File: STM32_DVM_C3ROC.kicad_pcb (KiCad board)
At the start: 4 copper layers, 110 x 56 mm, 174 parts, among them IC2 MCP6002, IC3 MCP6002, IC4 MCP6002, J1 40HAT, J2 USB_B_Micro, Q1 Crystal_GND24, SW1 SW_Push, T1 MMUN2214, T2 MMUN2214, T3 MMUN2214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

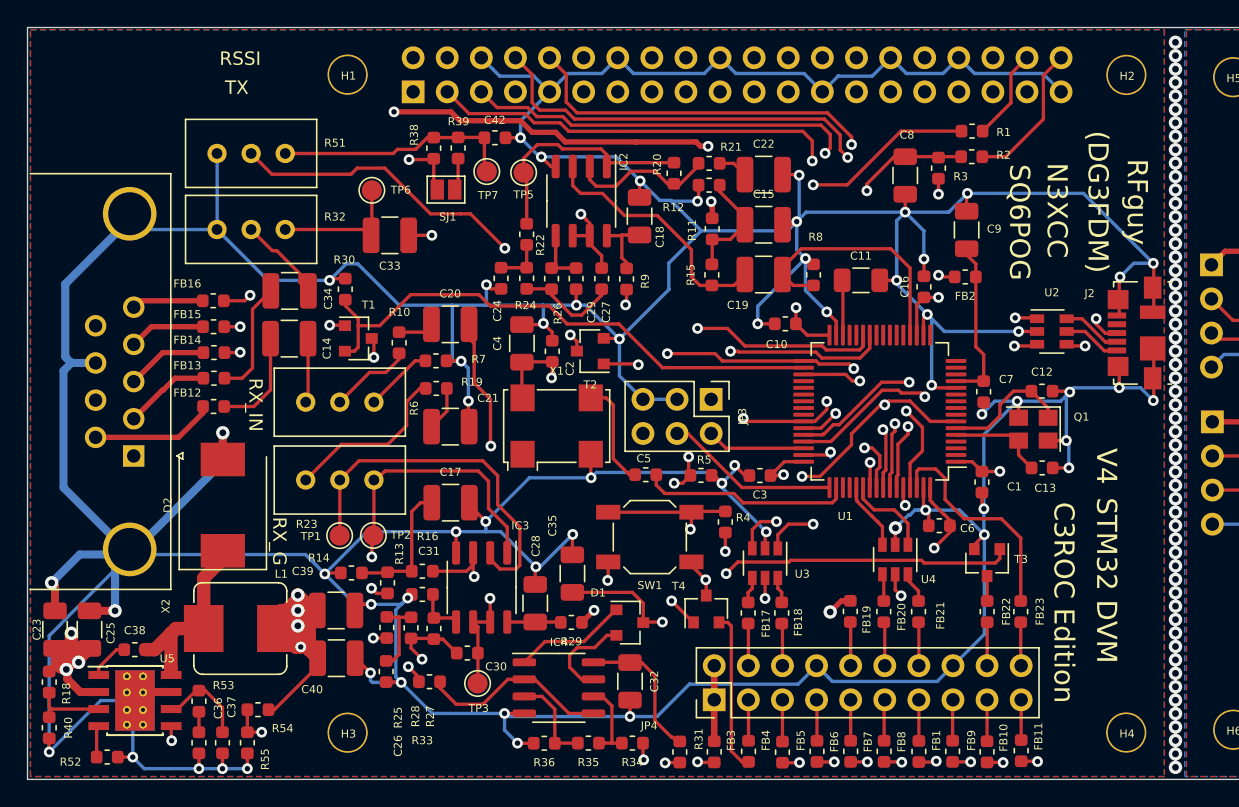
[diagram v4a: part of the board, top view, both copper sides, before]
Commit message: Layout fertig, Produktionsdaten für JCLPCB erzeugt
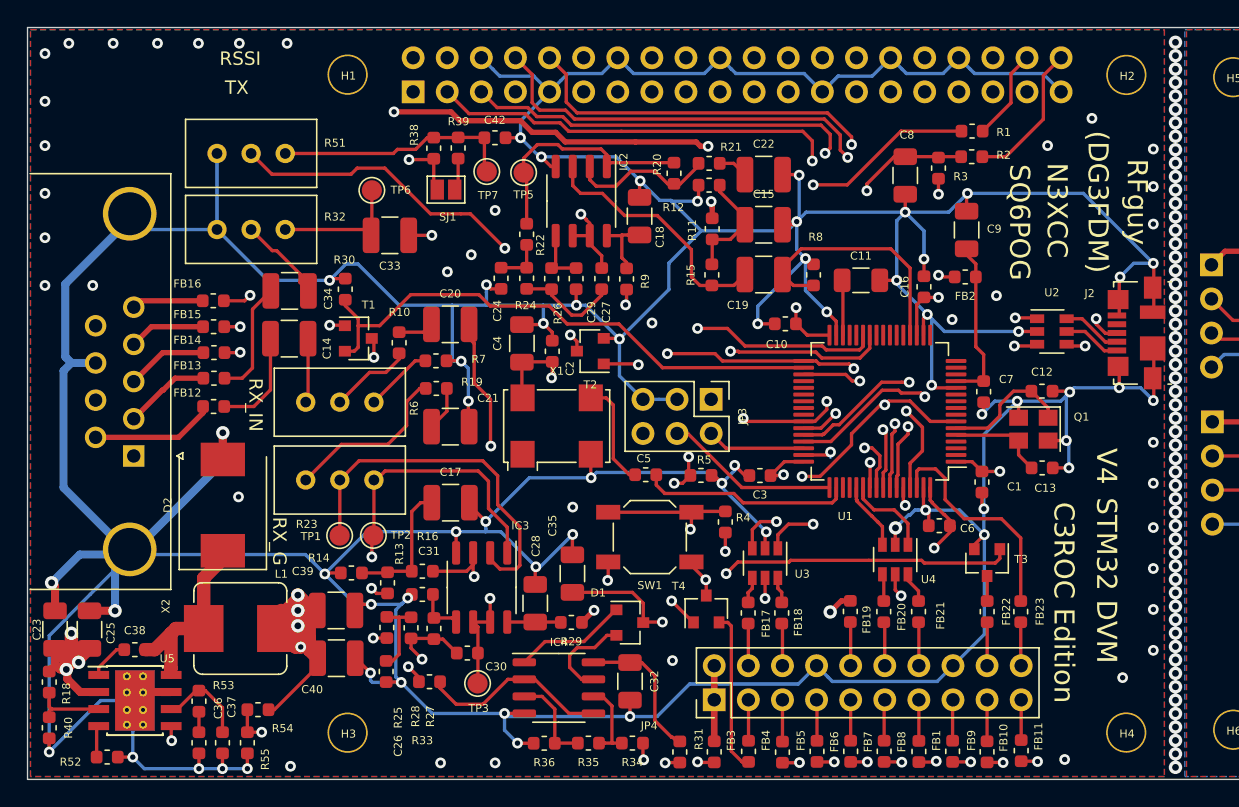
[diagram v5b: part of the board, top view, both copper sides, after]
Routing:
- net GND: vias 61 -> 98
- net (no net): vias 55 -> 56
- added copper zone on In1.Cu, net GND
